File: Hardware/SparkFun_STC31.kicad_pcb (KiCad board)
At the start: 2 copper layers, 25.4 x 25.4 mm, 47 parts, among them J3 Qwiic_RA, J4 I2C, J5 Qwiic_RA, U1 STC31, U2 SHTC3

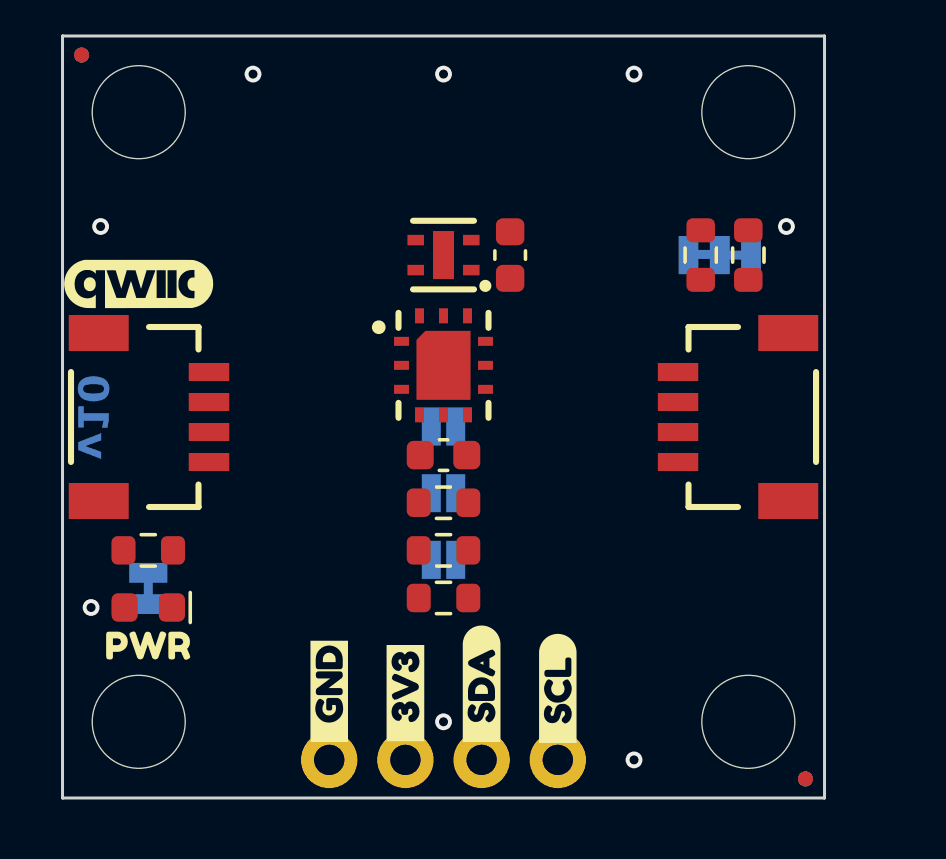
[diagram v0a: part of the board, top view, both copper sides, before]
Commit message: Routes most air-wires
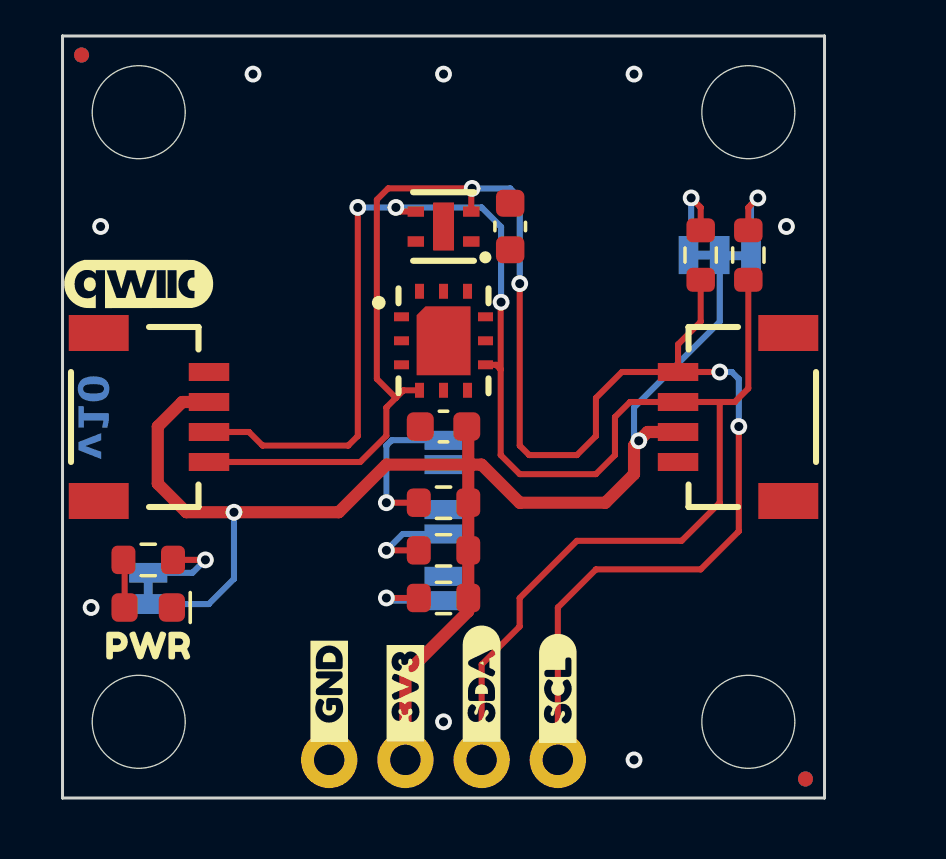
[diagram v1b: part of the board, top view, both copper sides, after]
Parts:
- moved C1 0.95 mm to (136.0, 98.4), turned to 180 degrees
- moved C3 0.95 mm to (138.2, 91.8), turned to -90 degrees
- moved JP4 0.95 mm to (136.0, 101.6), turned to 90 degrees
- moved JP5 0.95 mm to (136.0, 103.8), turned to 90 degrees
- moved U2 0.95 mm to (136.0, 91.8)
- moved JP3 0.86 mm to (136.0, 99.3), turned to -90 degrees
- moved U1 0.82 mm to (136.0, 95.6)
- moved R9 0.32 mm to (126.1, 102.9), turned to 180 degrees
- turned JP1 to -90 degrees
- turned JP2 to 0 degrees
- turned R1 to 180 degrees
- turned R4 to 180 degrees
- turned R5 to 180 degrees
- turned R8 to -90 degrees
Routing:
- net SCL: track 0.00 -> 59.6 mm, vias 0 -> 4
- net SDA: track 0.00 -> 58.2 mm, vias 0 -> 3
- net 3.3V: track 0.00 -> 49.8 mm, vias 0 -> 2
- net Net-(JP3-A): track 0.00 -> 4.96 mm, vias 0 -> 1
- net Net-(JP2-C): track 0.00 -> 3.21 mm, vias 0 -> 1
- net Net-(JP4-A): track 0.00 -> 3.21 mm, vias 0 -> 1
- net Net-(JP1-A): track 0.00 -> 3.16 mm, vias 0 -> 1
- net Net-(JP2-A): track 0.00 -> 3.15 mm, vias 0 -> 1
- net Net-(JP5-A): track 0.00 -> 3.02 mm, vias 0 -> 1
- net Net-(D1-A): track 0.00 -> 1.60 mm

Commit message: Routes a few more air-wires
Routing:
- net GND: track 0.07 -> 3.42 mm, vias 8 -> 18
- net 3.3V: track 49.8 -> 52.9 mm
- net SDA: track 58.2 -> 56.6 mm
